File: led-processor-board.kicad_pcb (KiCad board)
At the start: 2 copper layers, 100 x 89.5 mm, 128 parts, among them J1 USB-C, J2 SPARE, J3 SWD, J4 12V IN, J5 OUT1, J6 OUT2, J7 OUT3, J8 OUT4, J9 WL_GPIO, SW1 TS-1088R-02526, SW2 TS-1088R-02526, U1 RP2350B, U2 NCP1117ST33T3G, U3 W25Q128JVSIQ, U4 APS6404L-3SQR-SN, U5 RM2, U6 DS3231SN, U7 TPS54202H, X1 12MHz

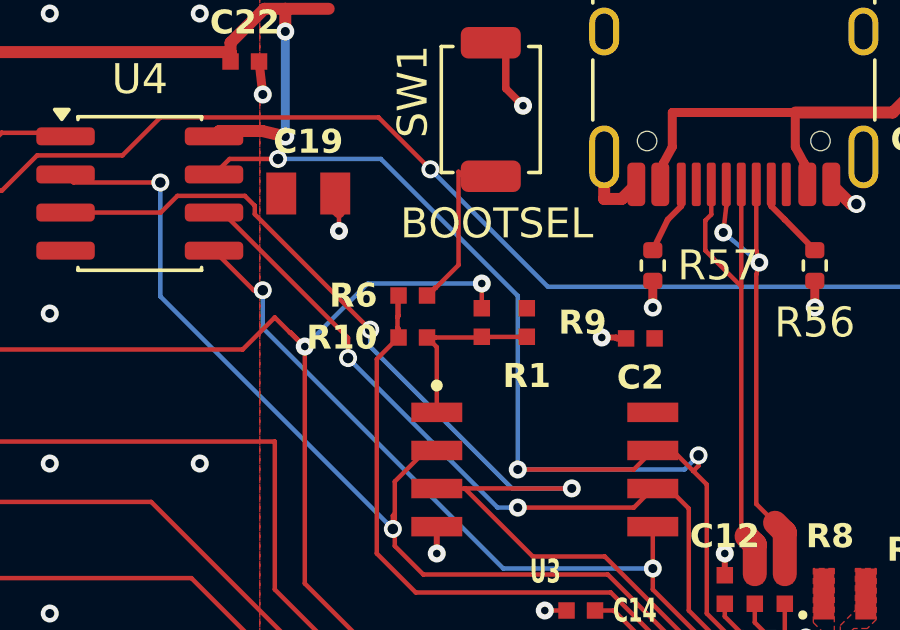
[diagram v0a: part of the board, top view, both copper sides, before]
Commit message: Remove R9 and the dead GPIO0 branch to it
R9 is Pi's unfitted 0R option from GPIO0 to the flash chip select. It was
DNP here too, so its only effect was a stub on OUT1's first data line.
Dropped from the schematic and board with its wiring; JLC files and
previews regenerated (assembly BOM/CPL unchanged).

Co-Authored-By: Claude Opus 5.5 (1M context) <noreply@anthropic.com>
Claude-Session: https://claude.ai/code/session_01CYnkeL97vxsPSCyXSKGro9
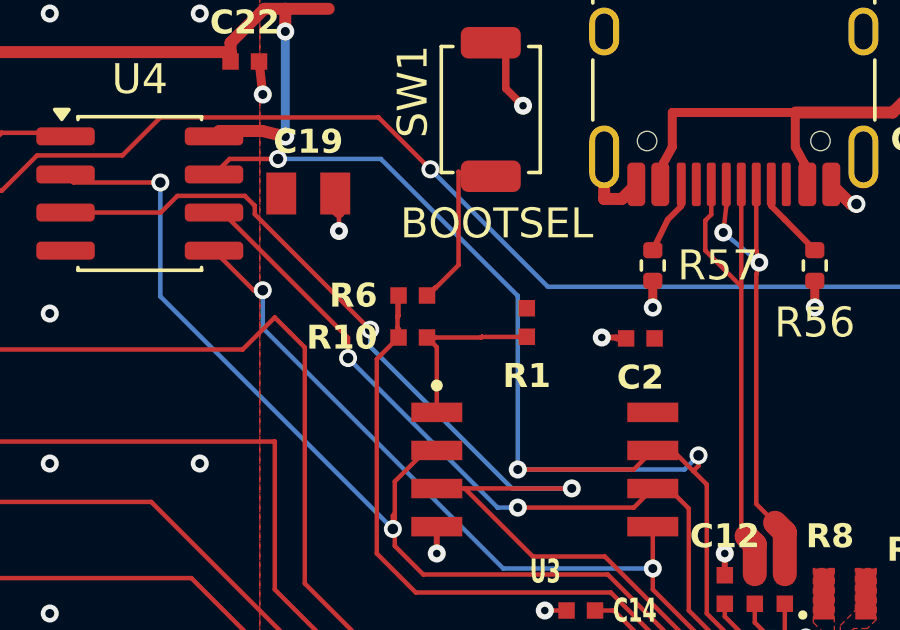
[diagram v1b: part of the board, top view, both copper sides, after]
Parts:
- removed R9: 0, RPI_COMPILED:generic_resc1005x35
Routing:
- net /GPIO0: track 51.0 -> 42.7 mm, vias 2 -> 0

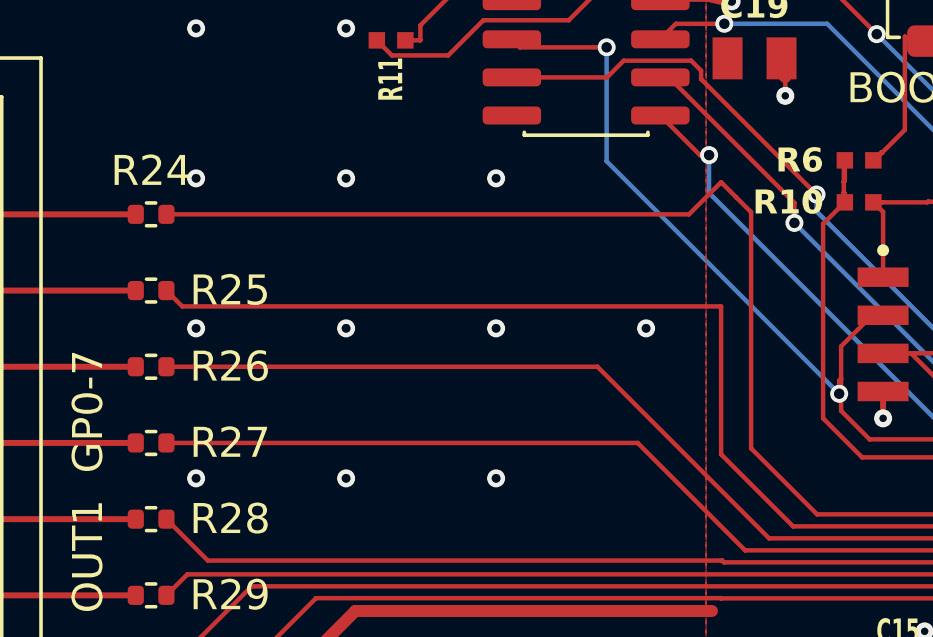
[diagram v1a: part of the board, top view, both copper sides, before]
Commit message: Straighten GPIO0 and chamfer GPIO1 on the way to OUT1
GPIO0 still jogged up to where R9's via was; it now runs straight to
OUT1's resistor. GPIO1's right-angle corner gets a 45-degree chamfer.

Co-Authored-By: Claude Opus 5.5 (1M context) <noreply@anthropic.com>
Claude-Session: https://claude.ai/code/session_01CYnkeL97vxsPSCyXSKGro9
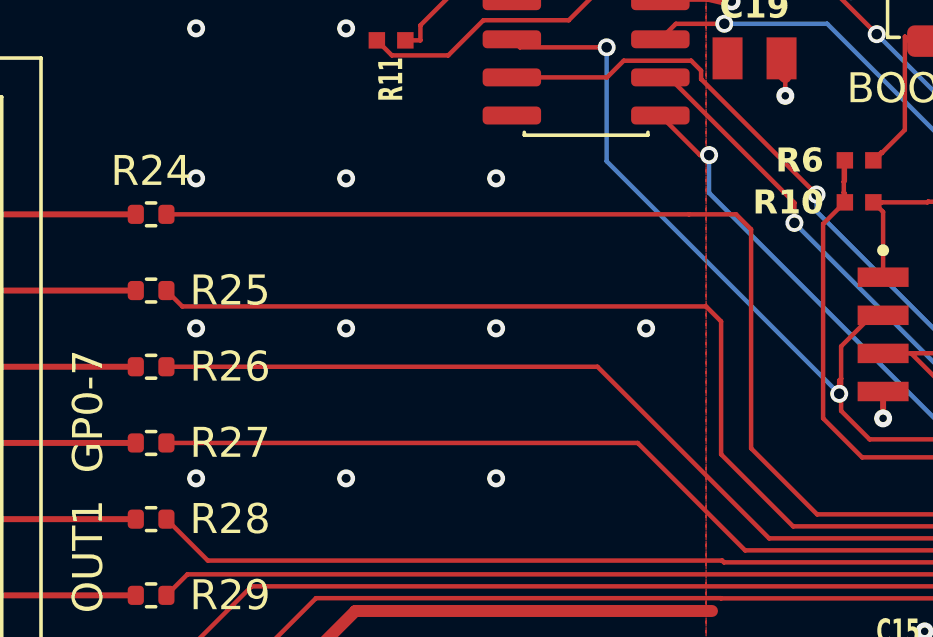
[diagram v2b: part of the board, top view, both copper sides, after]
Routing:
- net /GPIO0: track 42.7 -> 41.5 mm
